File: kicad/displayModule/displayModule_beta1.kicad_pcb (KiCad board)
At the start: 2 copper layers, 13 parts, among them J1 Connector, Q1 2N7000, Q2 2N7000, Q3 2N7000, Q4 2N7000, Q5 2N7000, Q6 2N7000, U1 ATtiny85-20PU, U2 74HC595, U3 74HC595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

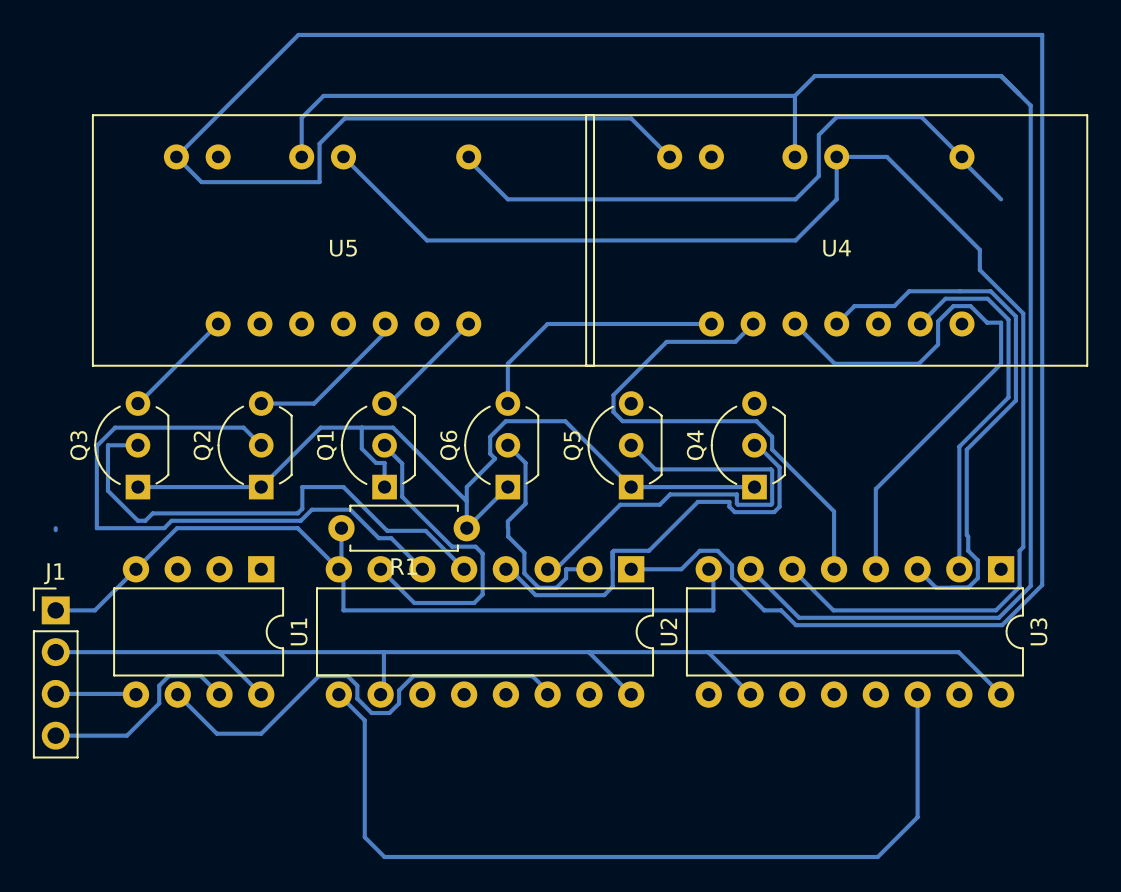
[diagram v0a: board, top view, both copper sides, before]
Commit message: Only activate squelch after AM transmission is picked up
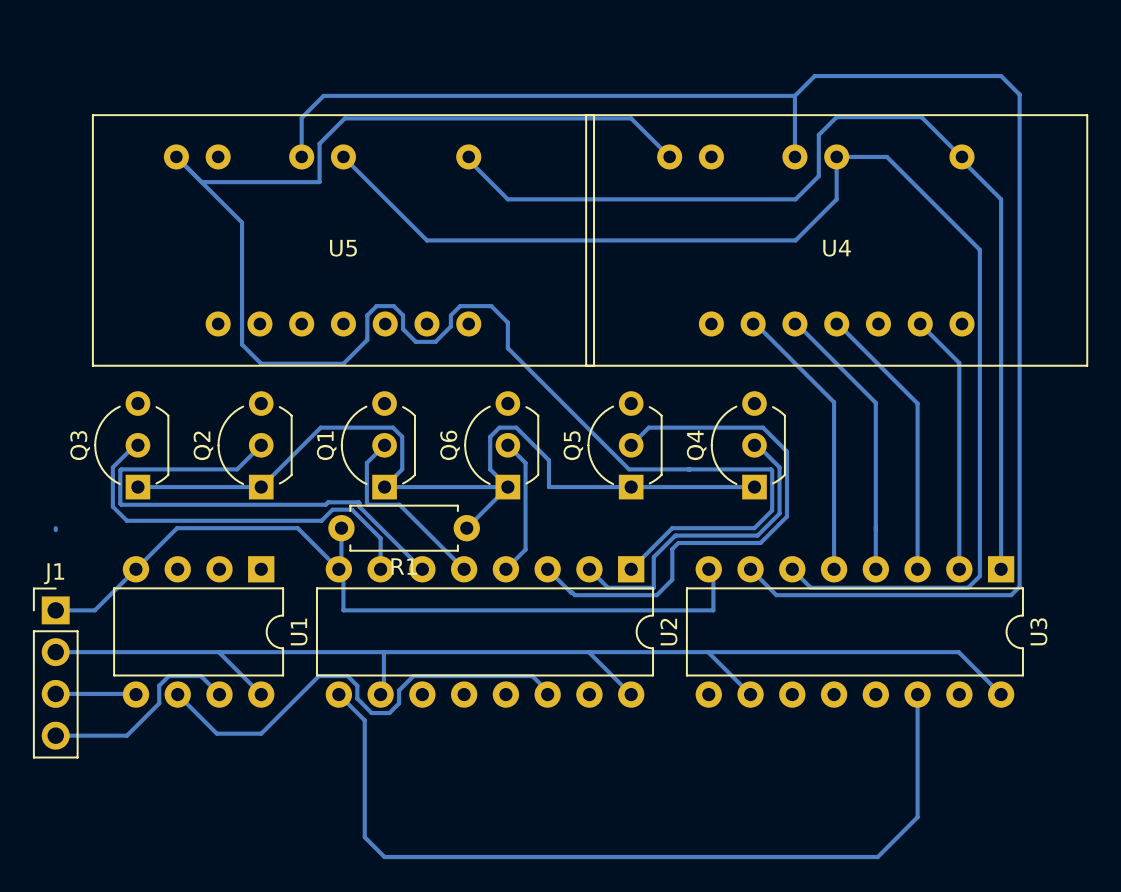
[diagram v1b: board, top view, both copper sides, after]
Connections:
- U2 pad 2: Net-(Q6-Pad2) -> Net-(Q4-Pad2)
- U2 pad 4: Net-(Q4-Pad2) -> Net-(Q6-Pad2)
- U2 pad 5: Net-(Q3-Pad2) -> Net-(Q1-Pad2)
- U2 pad 7: Net-(Q1-Pad2) -> Net-(Q3-Pad2)
- U4 pad 1: Net-(Q6-Pad3) -> Net-(Q1-Pad3)
- U4 pad 5: Net-(Q5-Pad3) -> Net-(Q2-Pad3)
- U4 pad 7: Net-(Q4-Pad3) -> Net-(Q3-Pad3)
- U5 pad 1: Net-(Q3-Pad3) -> Net-(Q4-Pad3)
- U5 pad 5: Net-(Q2-Pad3) -> Net-(Q5-Pad3)
- U5 pad 7: Net-(Q1-Pad3) -> Net-(Q6-Pad3)
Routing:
- net Net-(U2-Pad1): track 152.6 -> 103.1 mm
- net Net-(U3-Pad1): track 39.3 -> 61.8 mm
- net Net-(U3-Pad3): track 35.3 -> 17.0 mm
- net Net-(U3-Pad4): track 34.5 -> 17.3 mm
- net Net-(Q6-Pad3): track 15.8 -> 0.00 mm
- net Net-(U3-Pad5): track 31.4 -> 17.1 mm
- net Net-(Q2-Pad3): track 9.85 -> 0.00 mm
- net Net-(Q1-Pad2): track 19.7 -> 11.6 mm
- net Net-(Q4-Pad2): track 27.7 -> 20.0 mm
- net Net-(Q1-Pad3): track 7.12 -> 0.00 mm
- net Net-(U3-Pad2): track 23.3 -> 16.3 mm
- net Net-(Q3-Pad2): track 30.9 -> 24.0 mm
- net Net-(Q3-Pad3): track 6.88 -> 0.00 mm
- net Net-(Q2-Pad2): track 37.7 -> 31.5 mm
- net Net-(Q6-Pad2): track 14.2 -> 8.60 mm
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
